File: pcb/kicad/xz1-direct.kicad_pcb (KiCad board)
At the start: 2 copper layers, 48 x 13.5 mm, 7 parts, among them J1 PJ-327A0-SMT, J2 PJ-327A0-SMT

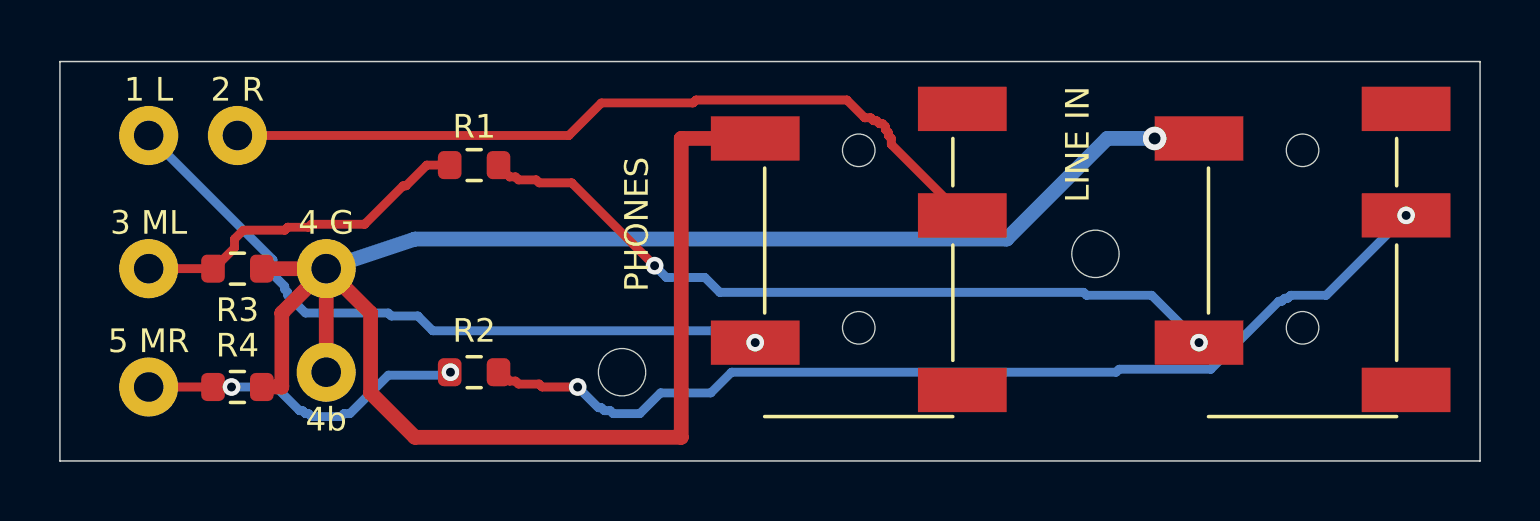
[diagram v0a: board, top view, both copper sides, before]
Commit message: pcb: Rev B-M2, two M2 mounting holes
The two 1.6 mm locating holes become 2.2 mm holes for M2 screws, with
a 5.2 mm copper keep-out, to mount the board in the first enclosure.

Co-Authored-By: Claude Opus 5.5 <noreply@anthropic.com>
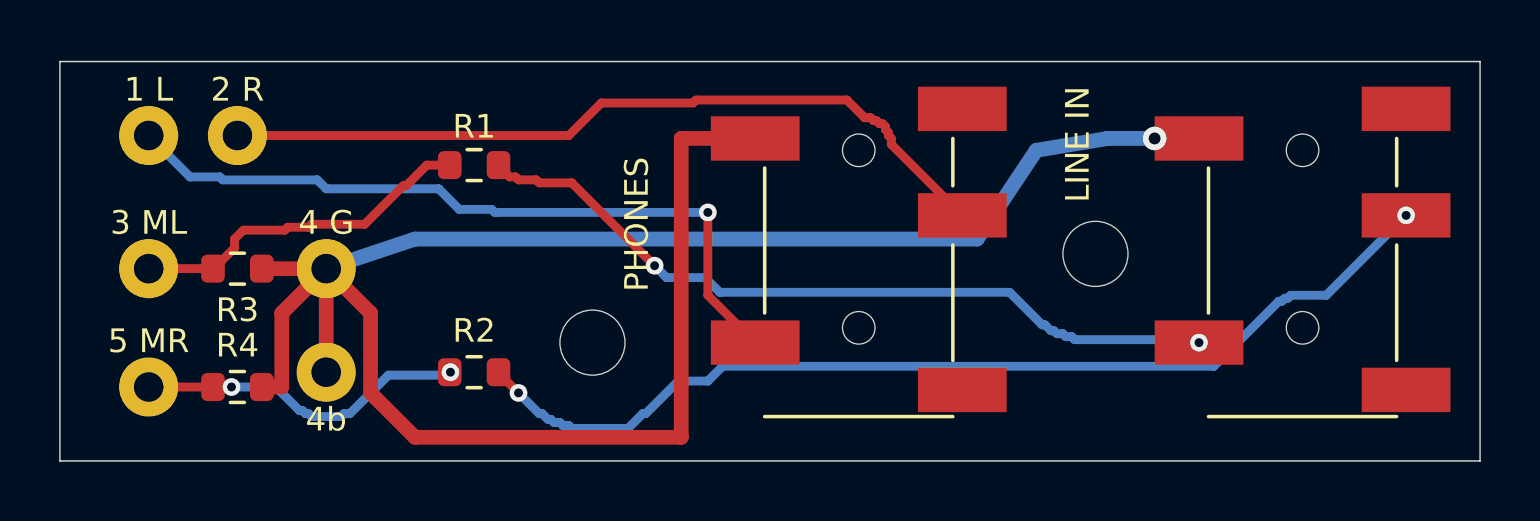
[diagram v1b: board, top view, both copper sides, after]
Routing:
- net /HP_L: track 23.8 -> 25.0 mm
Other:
- board text added: "XZ1 B-M2 48x13.5"
- board text removed: "XZ1 B / 48x13.5"

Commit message: pcb: Rev C-M2, jacks grouped next to the plug
Shorter lever on the plug when cables are plugged in: both jacks move
next to the plug, the wire pads move to the right, R1/R2 rotate and
the M2 holes move. Circuit, star ground and rules unchanged.

Co-Authored-By: Claude Opus 5.5 <noreply@anthropic.com>
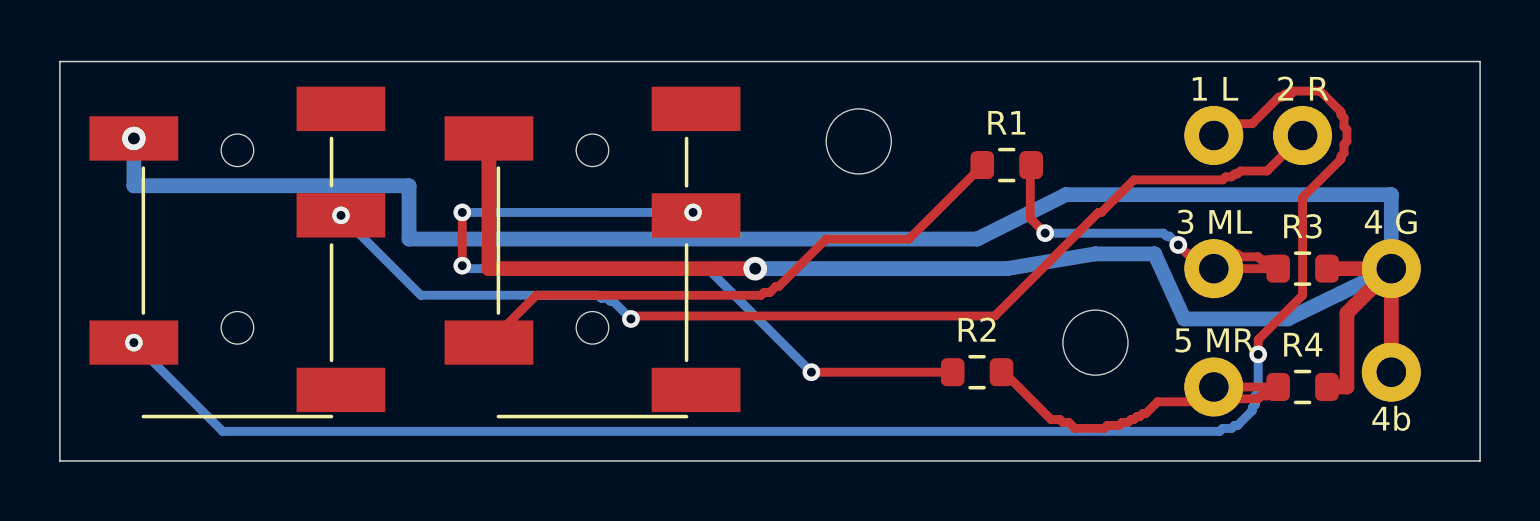
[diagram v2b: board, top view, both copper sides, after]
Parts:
- moved R3 36.0 mm to (42.0, 7.00)
- moved R4 36.0 mm to (42.0, 11.0)
- moved J2 24.0 mm to (18.0, 6.00)
- moved J1 21.0 mm to (6.00, 6.00)
- moved R1 18.0 mm to (32.0, 3.50), turned to 180 degrees
- moved R2 17.0 mm to (31.0, 10.5), turned to 180 degrees
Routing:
- net /HP_L: track 25.0 -> 56.1 mm, vias 1 -> 2
- net /GND: track 70.8 -> 96.5 mm, vias 1 -> 2
- net /HP_R: track 26.8 -> 36.5 mm, vias 0 -> 2
- net /LINE_L: track 26.2 -> 19.2 mm, vias 2 -> 0
- net /LINE_R: track 34.5 -> 27.9 mm, vias 2 -> 4
- net /MIC_R: track 11.3 -> 13.0 mm, vias 2 -> 0
- net /MIC_L: track 11.9 -> 13.2 mm, vias 0 -> 2
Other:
- board text added: "STAR GND"
- board text added: "XZ1 C-M2"
- board text removed: "STAR GND - NO POUR"
- board text removed: "XZ1 B-M2 48x13.5"
